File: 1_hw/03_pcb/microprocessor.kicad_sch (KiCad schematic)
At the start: 31 parts, among them U3 STM32F446ZETx, Y2 32.768k

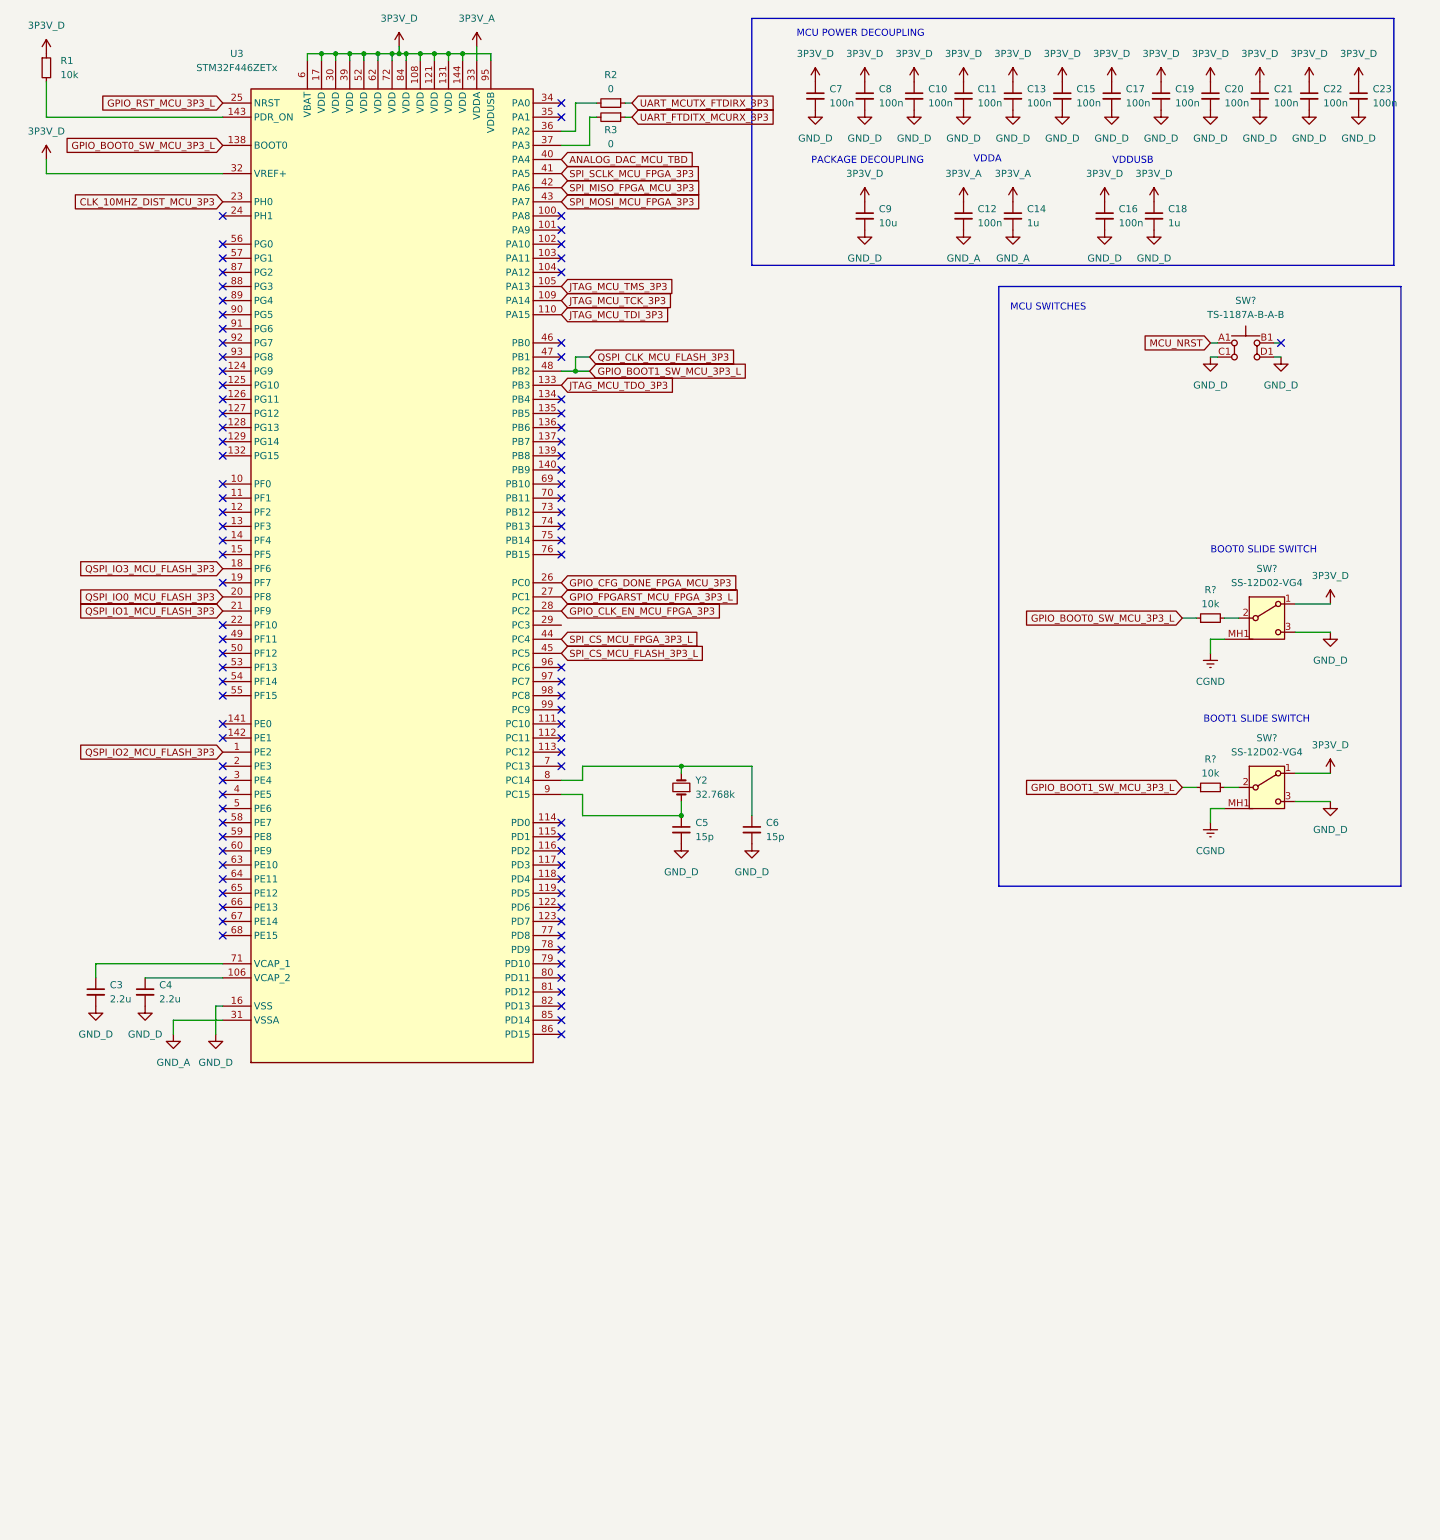
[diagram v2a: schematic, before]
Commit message: FEAT: Simulated Analog Paths, added first stage analog amp to schematic.
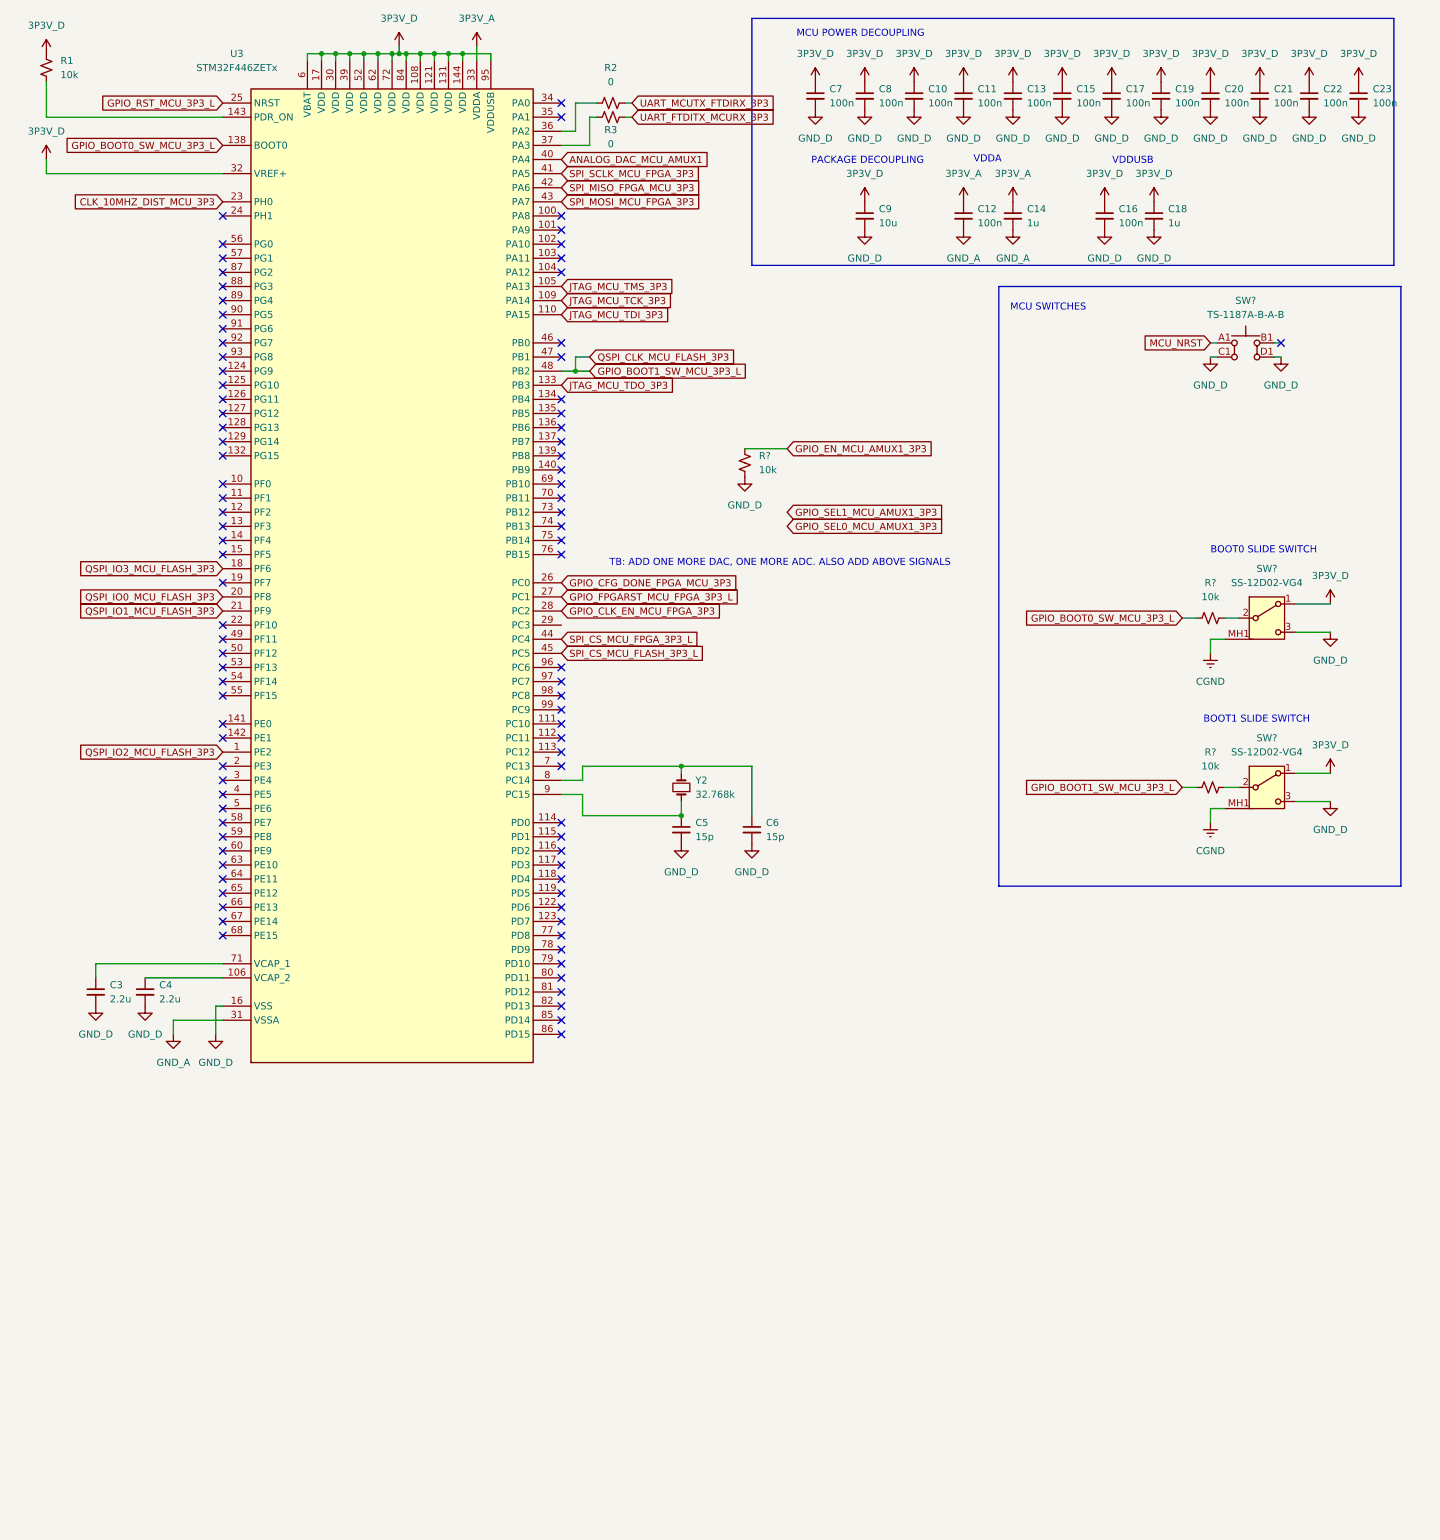
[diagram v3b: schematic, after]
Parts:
- removed R2, R3: 0, Resistor_SMD:R_0603_1608Metric, symbol Device:R_Small
- added R2, R3: 0, Resistor_SMD:R_0603_1608Metric, symbol Device:R_Small_US
- added R?: 10k, Resistor_SMD:R_0603_1608Metric, symbol Device:R_Small_US
- R1, R? (x2): symbol Device:R_Small -> Device:R_Small_US
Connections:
- net GND_D: now also R?.1
- net UART_FTDITX_MCURX_3P3: now also R3.2
- net UART_MCUTX_FTDIRX_3P3: now also R2.2
- net at U3.37 (PA3): now also R3.1
- net at U3.36 (PA2): now also R2.1
- net ANALOG_DAC_MCU_TBD renamed ANALOG_DAC_MCU_AMUX1
- new net GPIO_EN_MCU_AMUX1_3P3: R?.2
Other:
- note added: "TB: ADD ONE MORE DAC, ONE MORE ADC. ALSO ADD ABOVE SIGNALS"

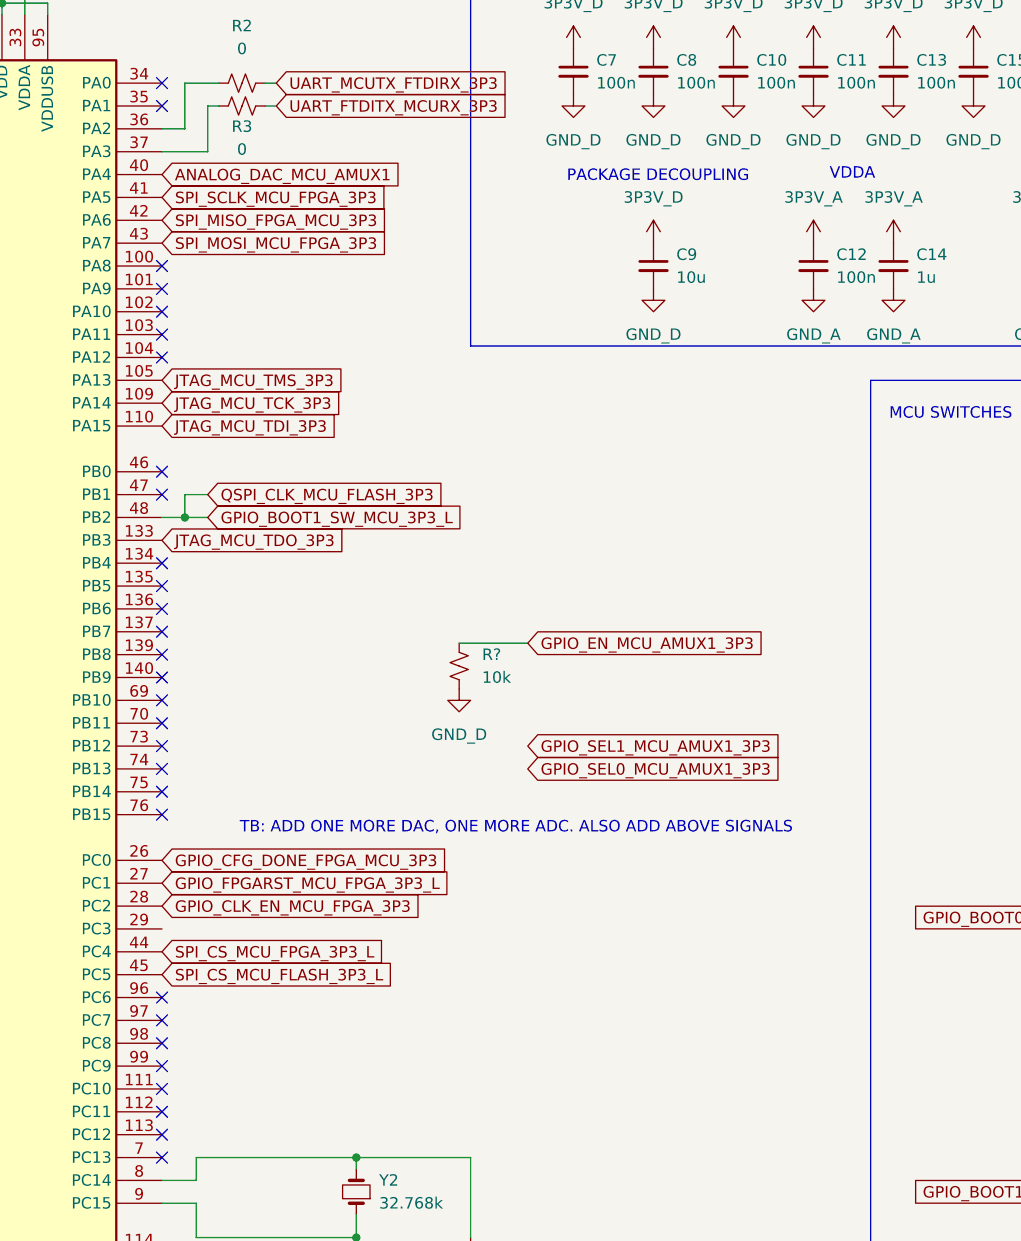
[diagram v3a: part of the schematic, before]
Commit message: FEAT: Added Analog Stage 2 to Schematic. Some additional symbols (Pot, SPDT Analog MUX, etc.) added to Project.
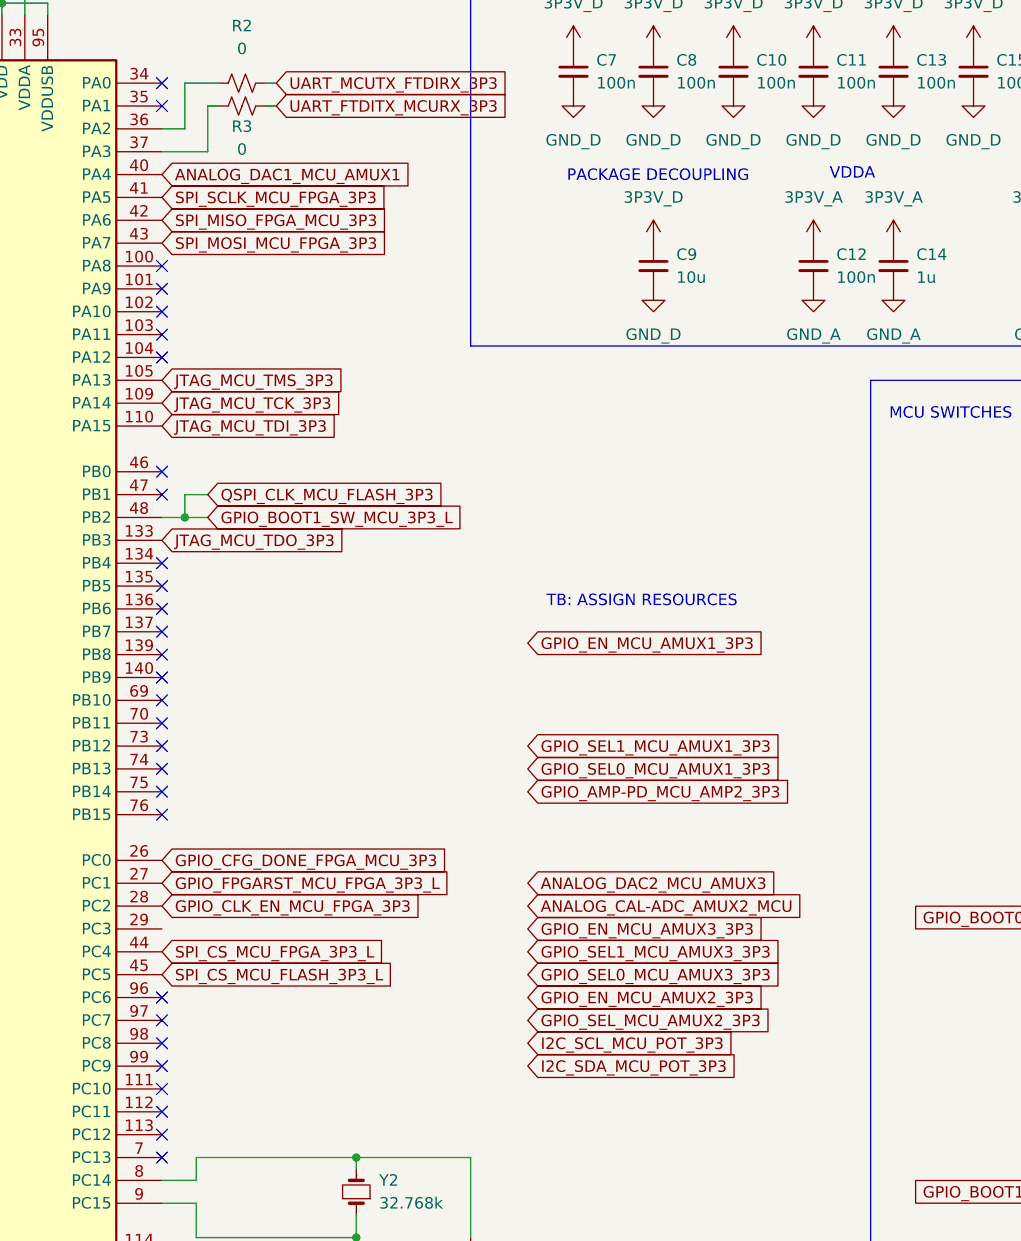
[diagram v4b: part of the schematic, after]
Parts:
- removed R?: 10k, Resistor_SMD:R_0603_1608Metric, symbol Device:R_Small_US
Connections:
- net ANALOG_DAC_MCU_AMUX1 renamed ANALOG_DAC1_MCU_AMUX1
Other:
- note added: "TB: ASSIGN RESOURCES"
- note removed: "TB: ADD ONE MORE DAC, ONE MORE ADC. ALSO ADD ABOVE SIGNALS"

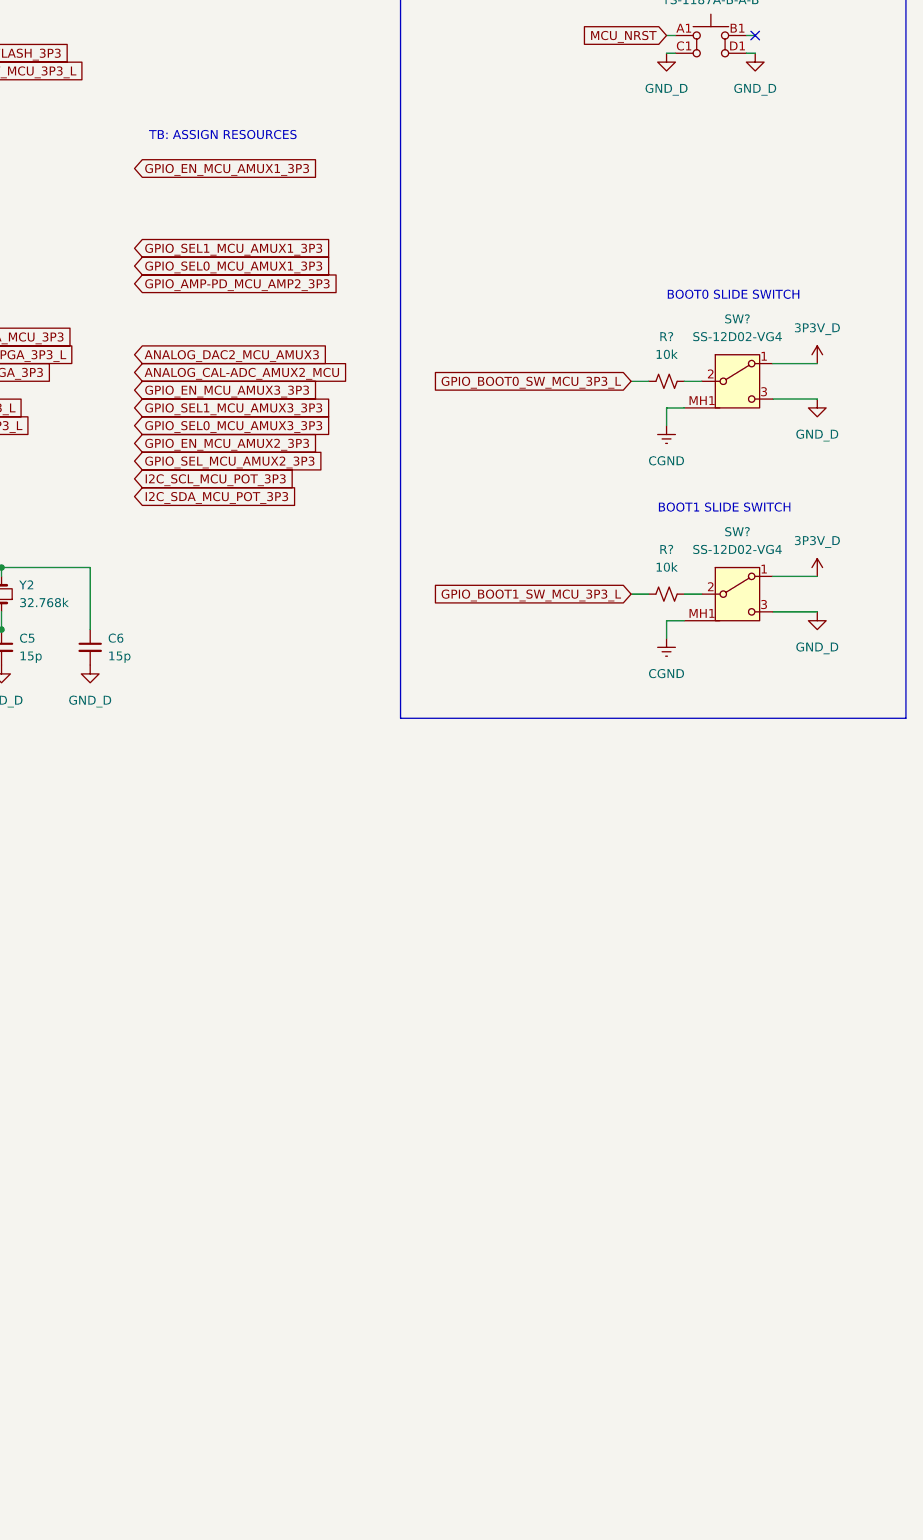
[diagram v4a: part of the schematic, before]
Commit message: FEAT: Swapped out DDS IC and connected. Started adding Clockign Components into Schematic.
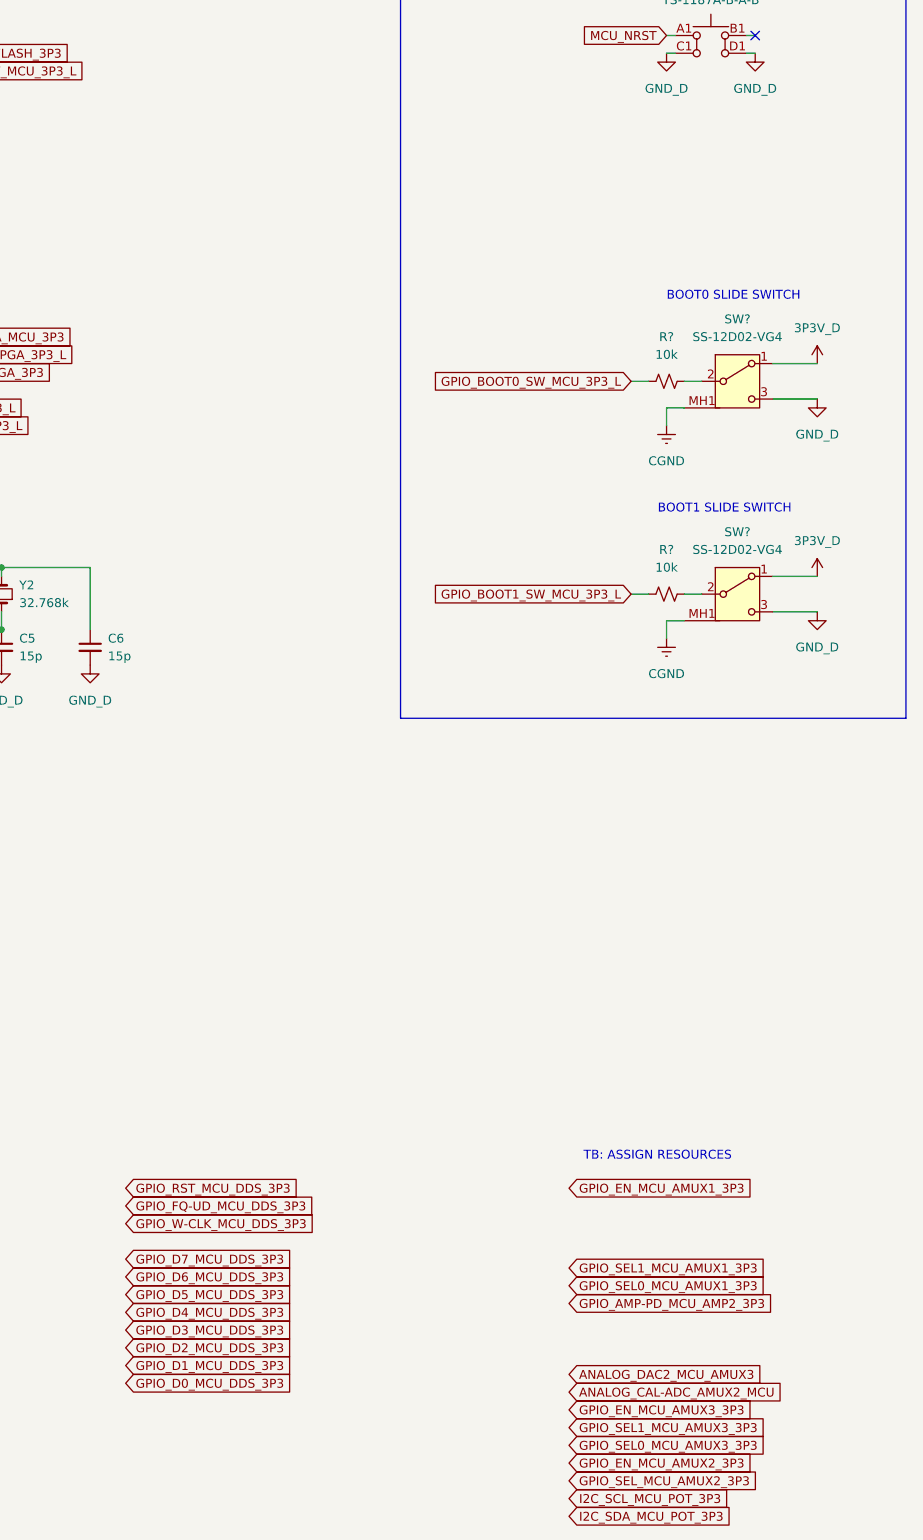
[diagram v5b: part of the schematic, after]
